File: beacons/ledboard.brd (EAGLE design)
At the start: 58.1 x 27.9 mm, 13 parts, among them Q1 2N3904, Q2 2N3904, Q3 2N3904

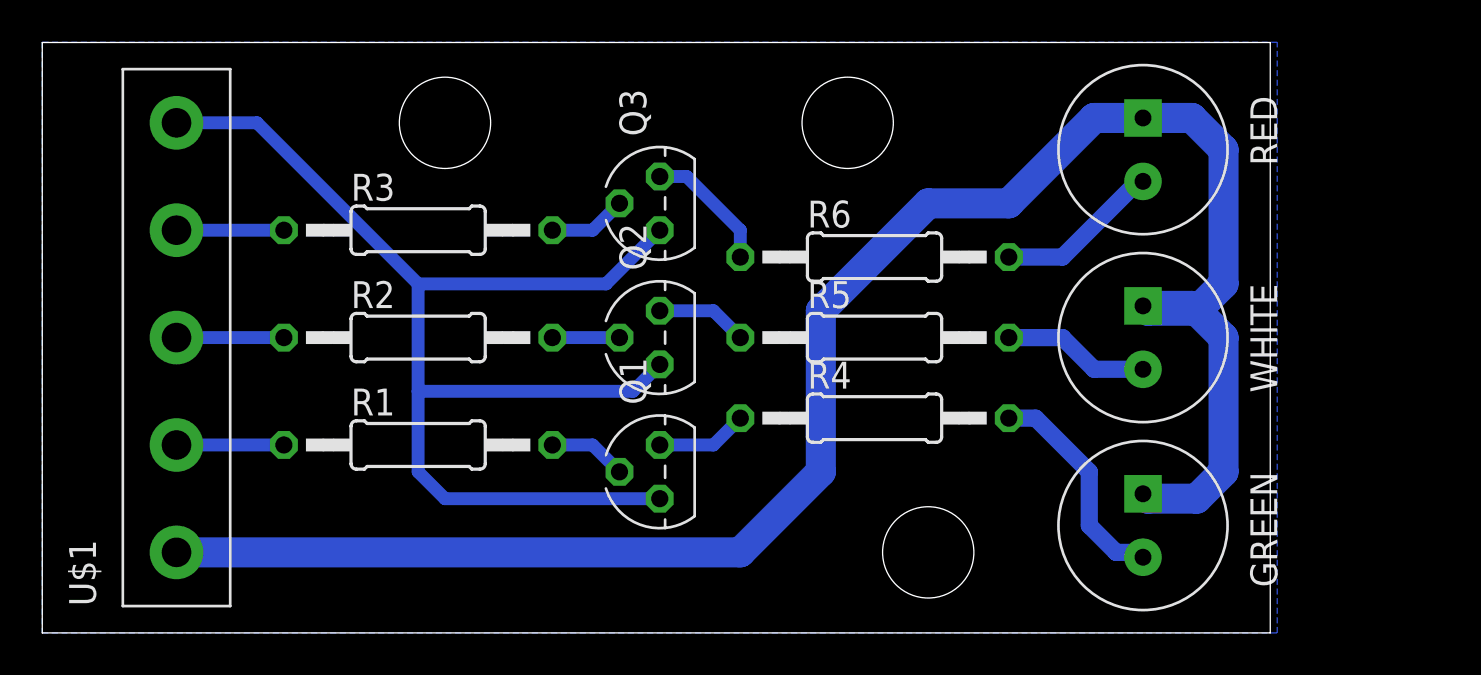
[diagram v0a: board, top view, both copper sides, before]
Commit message: Added phototransistor
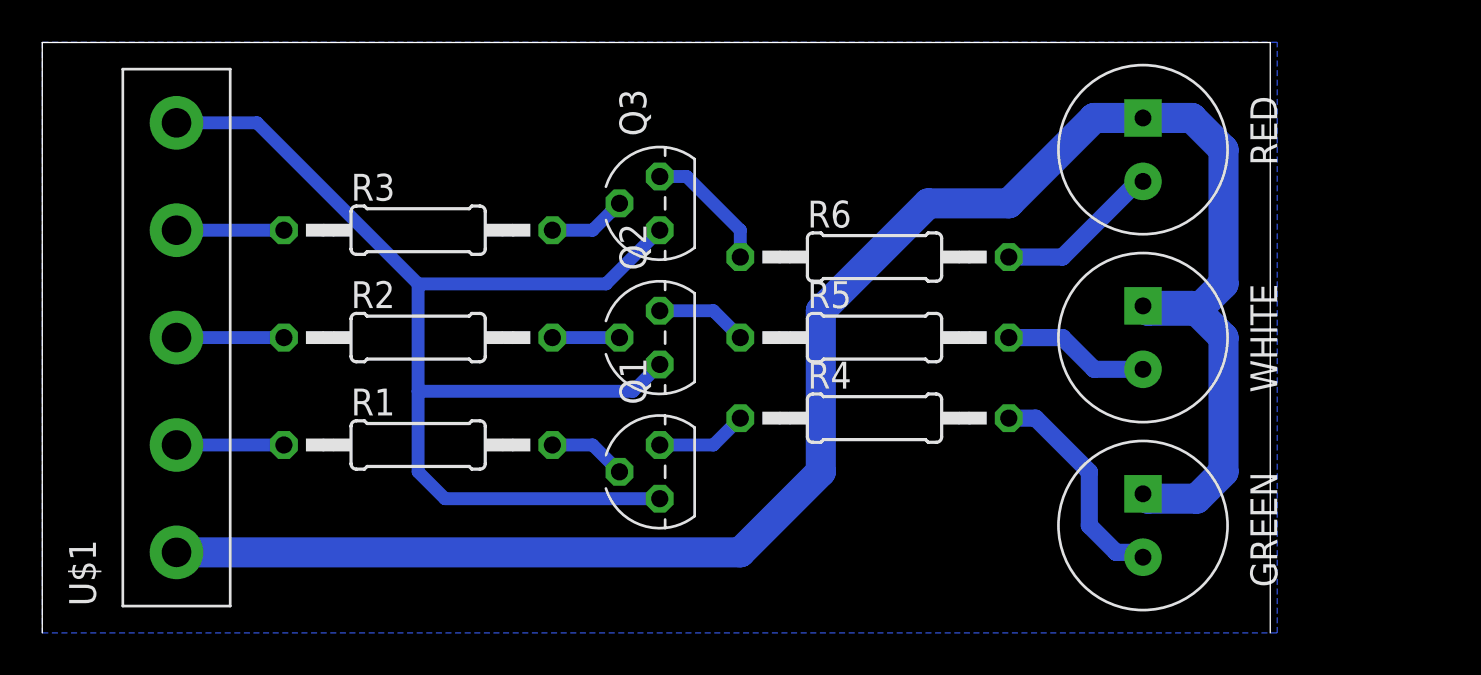
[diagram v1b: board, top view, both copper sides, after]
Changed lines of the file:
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@@
 <board>
 <plain>
-<wire x1="0" y1="0" x2="58.09" y2="0" width="0" layer="20"/>
 <wire x1="58.09" y1="0" x2="58.09" y2="27.93" width="0" layer="20"/>
 <wire x1="58.09" y1="27.93" x2="0" y2="27.93" width="0" layer="20"/>
 <wire x1="0" y1="27.93" x2="0" y2="0" width="0" layer="20"/>
-<hole x="19.05" y="24.13" drill="4.318"/>
-<hole x="41.91" y="3.81" drill="4.318"/>
-<hole x="38.1" y="24.13" drill="4.318"/>
 </plain>
 <attributes>

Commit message: Added switches for mode control
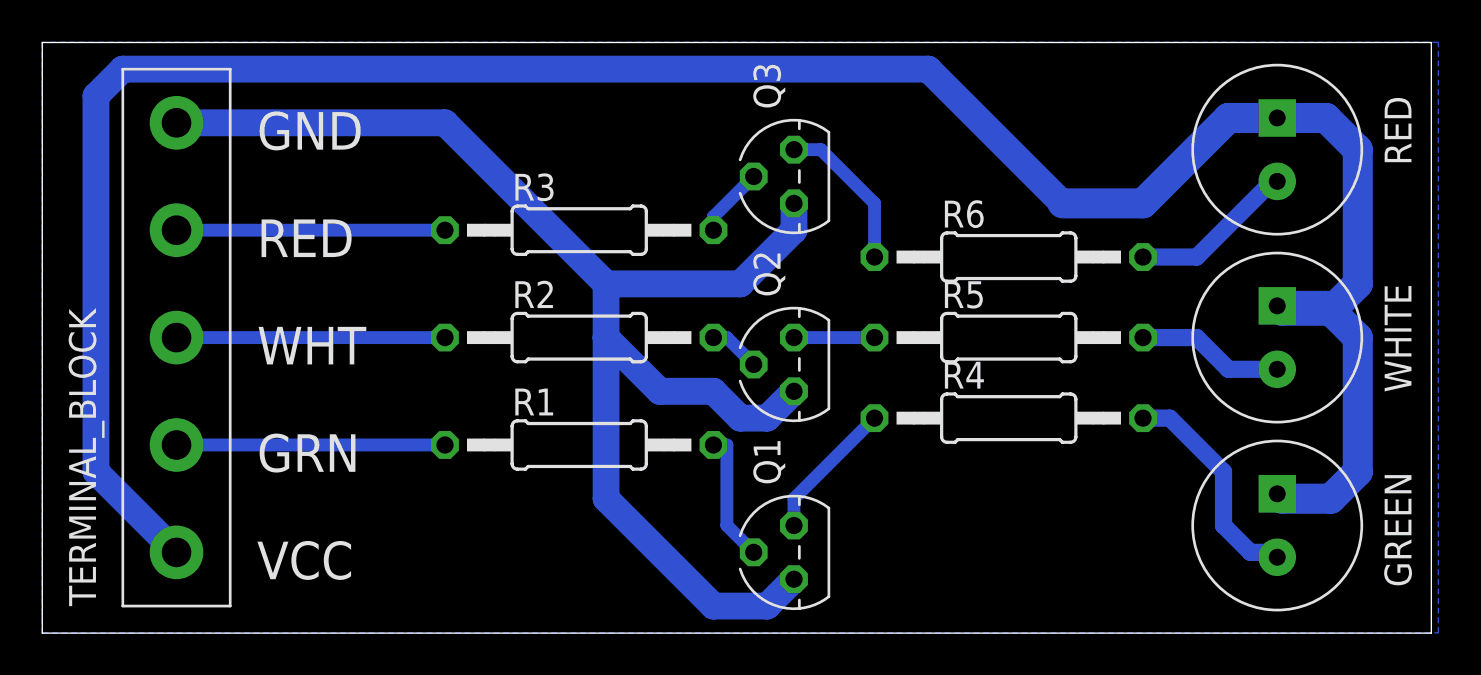
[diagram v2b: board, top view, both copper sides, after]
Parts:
- moved R1 7.62 mm to (25.4, 8.89)
- moved R2 7.62 mm to (25.4, 14.0)
- moved R3 7.62 mm to (25.4, 19.1)
- moved Q1 7.41 mm to (35.6, 3.81)
- moved Q2 6.48 mm to (35.6, 12.7)
- moved Q3 6.48 mm to (35.6, 21.6)
- moved GREEN 6.35 mm to (58.4, 5.08)
- moved R4 6.35 mm to (45.7, 10.2)
- moved R5 6.35 mm to (45.7, 14.0)
- moved R6 6.35 mm to (45.7, 17.8)
- moved RED 6.35 mm to (58.4, 22.9)
- moved WHITE 6.35 mm to (58.4, 14.0)
- renumbered U$1 to TERMINAL_BLOCK
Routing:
- net VCC: track 89.1 -> 114.3 mm
- net N$12: track 5.08 -> 12.7 mm
- net N$11: track 5.08 -> 12.7 mm
- net N$10: track 5.08 -> 12.7 mm
- net GND: track 59.9 -> 67.4 mm
- net N$1: track 3.70 -> 6.24 mm
- net N$4: track 4.34 -> 6.66 mm
- net N$6: track 6.13 -> 7.40 mm
- net N$2: track 3.18 -> 2.43 mm
- net N$5: track 4.34 -> 3.81 mm
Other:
- board size 58.1 x 27.9 mm -> 65.7 x 27.9 mm
- board text added: "GND"
- board text added: "GRN"
- board text added: "RED"
- board text added: "VCC"
- board text added: "WHT"
